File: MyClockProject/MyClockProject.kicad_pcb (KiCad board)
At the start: 2 copper layers, 19 parts, among them J1 Conn_01x16_Socket_ESP32, J2 Conn_01x16_Socket_ESP32, J2 USB_C_Receptacle_PowerOnly_6P, J4 RJ45, J5 Conn_01x05_Socket, J7 Barrel_Jack, J8 Conn_01x03_Socket, U1 ULN2003A

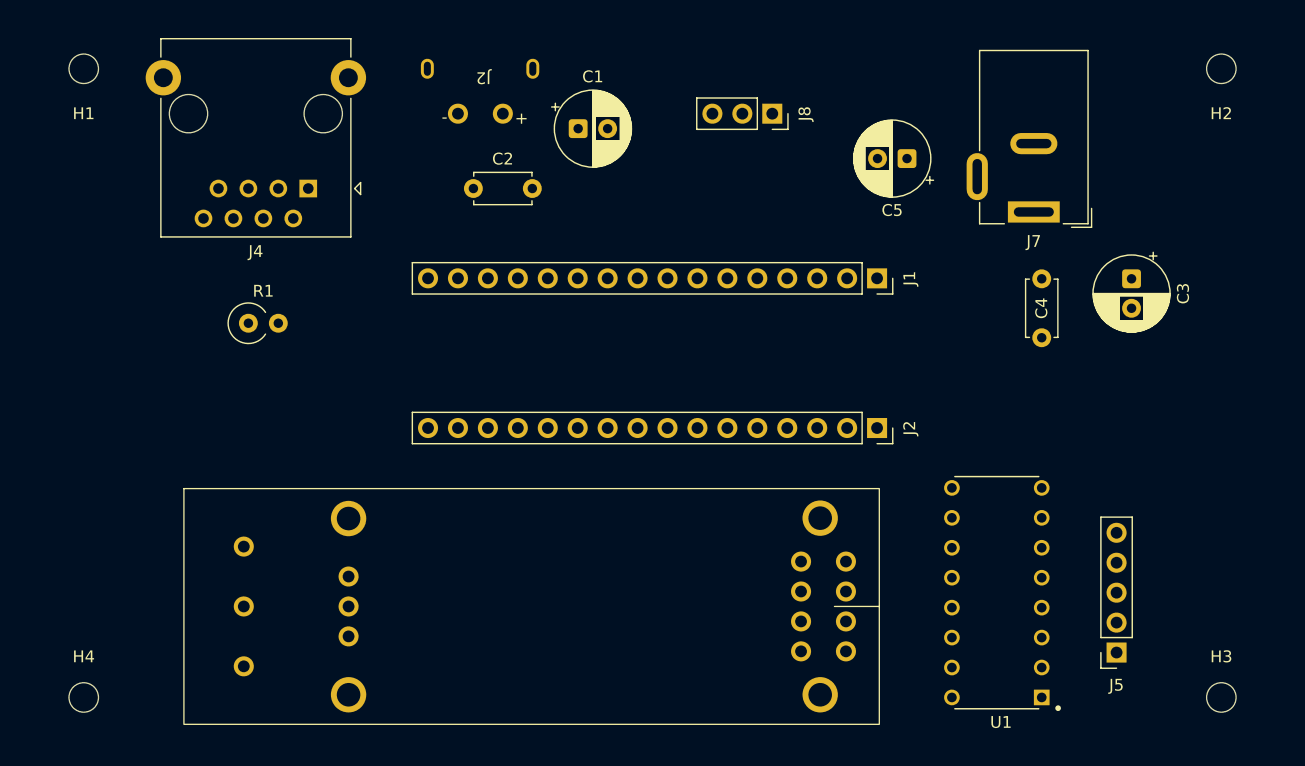
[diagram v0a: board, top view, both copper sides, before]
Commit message: 基盤を完成しました。５Vからのコンデンサの配線を修正しました。ホールセンサーを接続できるようにしました。
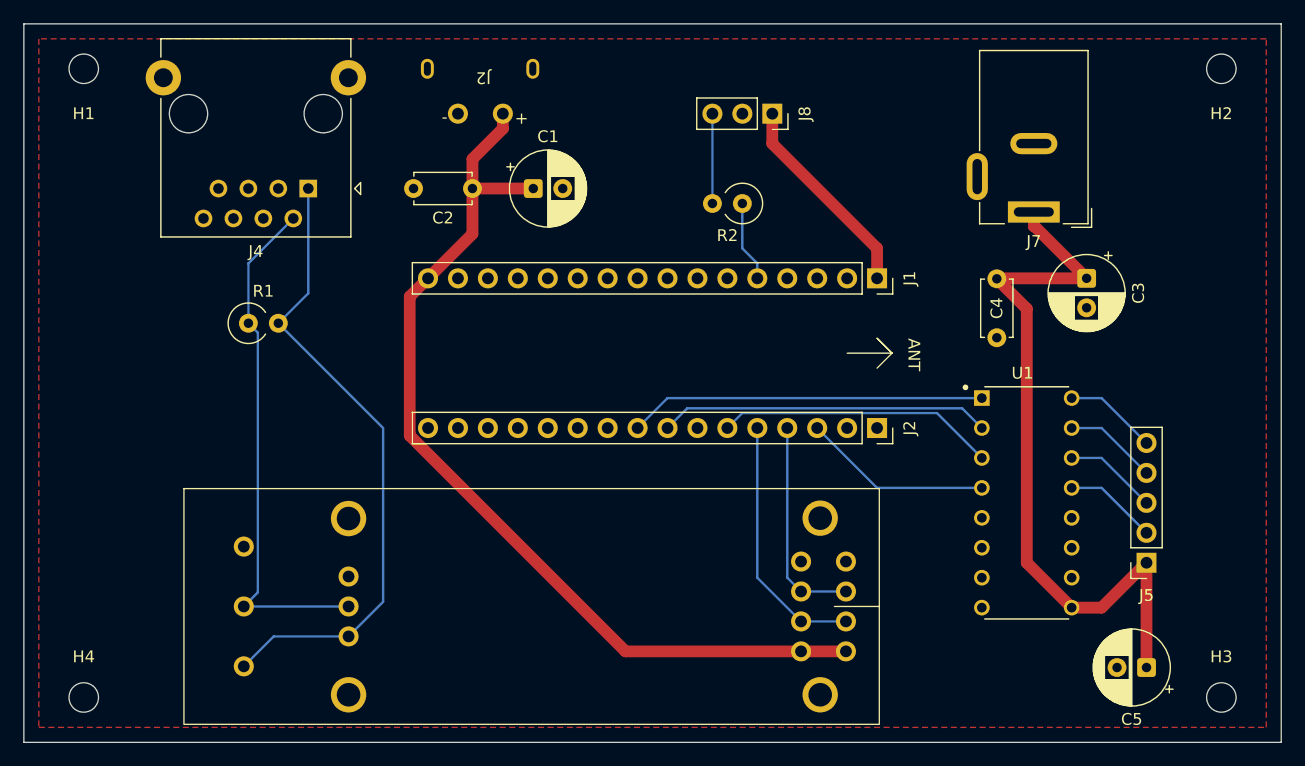
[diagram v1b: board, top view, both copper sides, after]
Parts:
- added R2: 10K, Resistor_THT:R_Axial_DIN0309_L9.0mm_D3.2mm_P2.54mm_Vertical, F.Cu at (144.8, 69.8)
- moved C5 47.7 mm to (179.1, 109.2)
- moved J5 8.03 mm to (179.1, 100.3)
- moved U1 8.03 mm to (168.9, 95.2), turned to 0 degrees
- moved C1 6.35 mm to (127.0, 68.6)
- moved C3 3.81 mm to (174.0, 76.2)
- moved C4 3.81 mm to (166.4, 76.2)
- moved C2 0.08 mm to (121.9, 68.6), turned to 180 degrees
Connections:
- C1 pad 1: Net-(C1-Pad1) -> Net-(J1_5V)
- C1 pad 2: Net-(C1-Pad2) -> GND
- C2 pad 1: Net-(C1-Pad2) -> Net-(J1_5V)
- C2 pad 2: Net-(J1-Pin_16) -> GND
- C3 pad 1: Net-(J5-Pin_5) -> Net-(J7-Pin_1)
- C4 pad 1: Net-(J5-Pin_5) -> Net-(J7-Pin_1)
- C5 pad 1: Net-(J5-Pin_5) -> Net-(J7-Pin_1)
- J1 pad 34: unconnected-(J1-Pin_6-Pad34) -> Net-(J1-Pin_34)
- J1 pad 3V3: unconnected-(J1-Pin_1-Pad3V3) -> Net-(J1-Pin_3V3)
- J2 pad 6: Net-(J2_5V) -> Net-(J1_5V)
- J5 pad 1: Net-(J5-Pin_1) -> Net-(J7-Pin_1)
- J5 pad 2: Net-(J5-Pin_2) -> Net-(U1-Pin_13)
- J5 pad 3: Net-(J5-Pin_3) -> Net-(U1-Pin_14)
- J5 pad 4: Net-(J5-Pin_4) -> Net-(U1-Pin_15)
- J5 pad 5: Net-(J5-Pin_5) -> Net-(U1-Pin_16)
- J7 pad 1: Net-(J5-Pin_5) -> Net-(J7-Pin_1)
- J8 pad 1: Net-(J1-Pin_1) -> Net-(J1-Pin_3V3)
- U1 pad 1: Net-(J5-Pin_1) -> Net-(J2_pin_18)
- U1 pad 13: Net-(J2-Pin_3) -> Net-(U1-Pin_13)
- U1 pad 14: Net-(J2-Pin_6) -> Net-(U1-Pin_14)
- U1 pad 15: Net-(J2-Pin_8) -> Net-(U1-Pin_15)
- U1 pad 16: Net-(J2-Pin_9) -> Net-(U1-Pin_16)
- U1 pad 2: Net-(J5-Pin_2) -> Net-(J2-Pin_19)
- U1 pad 3: Net-(J5-Pin_3) -> Net-(J2-Pin_21)
- U1 pad 4: Net-(J5-Pin_4) -> Net-(J2-Pin_22)
- U1 pad 9: Net-(J5-Pin_5) -> Net-(J7-Pin_1)
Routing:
- net Net-(J1_5V): track 0.00 -> 80.3 mm
- net Net-(J7-Pin_1): track 0.00 -> 62.5 mm
- net Net-(U3-OUT1): track 0.00 -> 53.9 mm
- net Net-(U3-OUT2): track 0.00 -> 44.2 mm
- net Net-(J2_pin_18): track 0.00 -> 30.3 mm
- net Net-(J2-Pin_19): track 0.00 -> 28.1 mm
- net Net-(J2-Pin_21): track 0.00 -> 23.7 mm
- net Net-(J2-Pin_RXI): track 0.00 -> 21.8 mm
- net Net-(J2-Pin_TXO): track 0.00 -> 18.2 mm
- net Net-(J1-Pin_3V3): track 0.00 -> 17.7 mm
- net Net-(J2-Pin_22): track 0.00 -> 16.1 mm
- net Net-(U1-Pin_16): track 0.00 -> 7.93 mm
- net Net-(U1-Pin_14): track 0.00 -> 7.93 mm
- net Net-(U1-Pin_13): track 0.00 -> 7.93 mm
- net Net-(U1-Pin_15): track 0.00 -> 7.93 mm
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- added copper zone on F.Cu, net GND
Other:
- board outline added: 106.7 x 61 mm
- board text added: "ANT"
